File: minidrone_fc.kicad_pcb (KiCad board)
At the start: 2 copper layers, 50 x 64 mm, 40 parts, among them J1 BATT, J2 MOTOR_FL, J3 MOTOR_FR, J4 MOTOR_RL, J5 MOTOR_RR, Q1 AO3400A, Q2 AO3400A, Q3 AO3400A, Q4 AO3400A, U1 XIAO_ESP32C3, U2 GY-521, U3 BMP280

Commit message: rev2.1: 昇降圧DC-DC(TPS63002)を追加し4層化
## なぜ

改訂前の基板には昇圧素子が1つもなく、電池電圧が「3.3V + LDOドロップアウト」
を下回れば 3V3 レールは必ず追従して下がる構造だった。
8520コアレスモーター4個で 6.5A を引くと電池は 3.7V→3.4V に沈み、
そこから D5(SS24) の 0.4V を引いて VMCU ≈ 3.0V、
さらに XIAO 内蔵 LDO のドロップアウトを引くと 3V3 は 2.8〜2.95V。
ESP32-C3 の動作下限 3.0V を公称電圧ですら下回っており、
スロットルを上げた瞬間に MCU がリセットする状態だった。

## 何を変えたか

- U4 TPS63002 (昇降圧・5V固定) を VBAT と XIAO の "5V" ピンの間に挿入
  L1 2.2uH / C10 10uF(in) / C11 22uF(out) / C12 0.1uF(VINA)
  電池 3.0V でも出力5V。D5 で 0.4V 落ちても 4.6V が XIAO に入り、
  内蔵LDO が 3.3V を作るのに必要な 3.5V に対し余裕1V以上
- D5 は流用。向きも不変で、上流が VBAT から V5V に変わっただけ
- 4層化: In1.Cu = ベタGND 全面 2949mm2 / In2.Cu = VBAT プレーン 全面 2811mm2
  6.5A を 0.6mm トレースで流していた状態を解消
- GND スティッチングビア 133本を衝突判定付きで自動配置
- U4 にローカルクリアランス 0.1mm を設定
  VSON-10 は 0.5mmピッチでパッド間 0.22mm しかなく、VBAT が属する
  Power ネットクラスの 0.25mm 要求を物理的に満たせないため。
  Power の 0.25mm はモーター大電流の配線・ベタ向けポリシーであり、
  ファインピッチICのピン間に適用する意図ではない (JLCPCB 製造限界 0.1mm)

+3V3 / VMCU / GATE_* / M_* / SCL / SDA は一切変更していない。
既存部品のパッド-ネット変更は D5 pad2 の VBAT→V5V ただ1箇所。

## 検証 (kicad-cli)

                    改訂前          改訂後
  DRC 違反          32 (warning)    37 (warning) ※増分5はすべてシルク重なり
  DRC エラー        0               0
  未配線            4               1  (改善)
  schematic_parity  0               0  (回路図と基板が完全一致)
  ERC               warning 5/err 0 warning 5/err 0 (同一)

## 残課題

- 未配線1件 (GNDベタの孤立島)。電気的な害はない
- シルク警告5件。C10/C11/C12 のリファレンス文字が隣接銅箔に重なる。
  この一角は部品とビアで埋まっており逃がす余地がない
- Gerber / BOM / 実装座標は未再出力。4層として出し直しが必要
- 実機でのブラウンアウト解消は未検証

詳細は README.md 第9節と docs/superpowers/plans/2026-09-19-buckboost-and-4layer.md

Co-Authored-By: Claude Opus 5 <noreply@anthropic.com>
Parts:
- added C10: 10u, Capacitor_SMD:C_0805_2012Metric, B.Cu at (11.9, 60.8)
- added C11: 22u, Capacitor_SMD:C_0805_2012Metric, B.Cu at (18.0, 60.8)
- added C12: 0.1u, Capacitor_SMD:C_0603_1608Metric, B.Cu at (11.7, 55.5)
- added L1: 2.2uH, Inductor_SMD:L_APV_ANR3015, B.Cu at (15.0, 60.9)
- added U4: TPS63002, Package_SON:VSON-10-1EP_3x3mm_P0.5mm_EP1.65x2.4mm_ThermalVias, B.Cu at (15.0, 56.6)
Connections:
- D5 pad 2: VBAT -> V5V
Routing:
- net V5V: track 0.00 -> 15.9 mm, vias 0 -> 2
- net SW_L1: track 0.00 -> 2.95 mm
- net SW_L2: track 0.00 -> 2.95 mm
- net VBAT: track 202.7 -> 205.2 mm, vias 0 -> 3
- net GND: vias 0 -> 140
- added copper zone on In1.Cu, net GND
- added copper zone on In2.Cu, net VBAT
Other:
- copper layers 2 -> 4

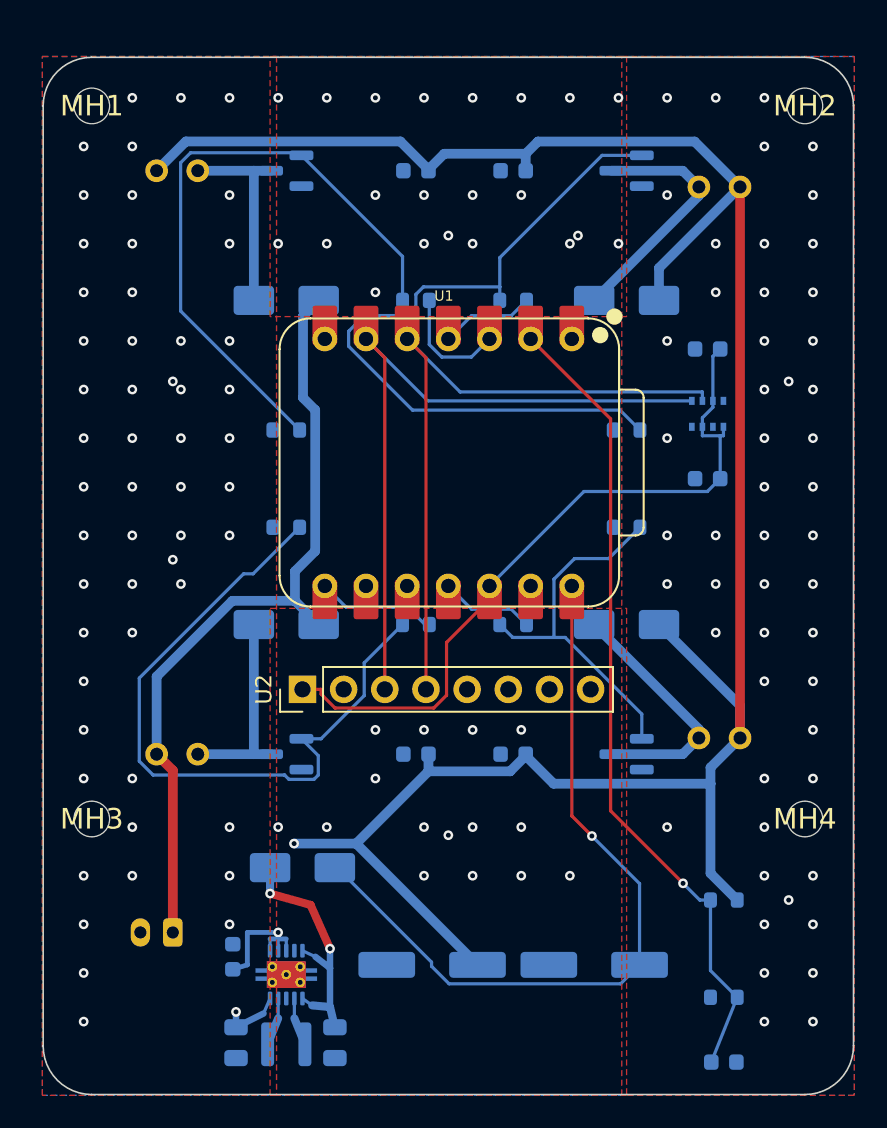
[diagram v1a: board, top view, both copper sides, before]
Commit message: rev3: 回路図を全面刷新し、29x29mm 4層基板の骨格を作成
rev2.1 (50x64mm / 取付穴44x44mm) を Tiny Whoop 標準ピッチに作り直す。
回路図は rev2 の内容を破棄して一から構成した（rev2.1 は main に保全）。

## 回路図（ERC エラー0 / 32ネット / 55部品）

  XIAO ESP32C3 (DIP) -> ESP32-C3-MINI-1 (SMD, 基板内蔵アンテナ)
  GY-521 モジュール   -> BMI270 直付け (SPI)
  BMP280              -> SPI に変更し IMU とバス共用
  TPS63002(5V)+LDO    -> TPS63001 で 3.3V 一段
  電解コンデンサ      -> 積層セラミック
  USB-C (TYPE-C-31-M-12) + USBLC6 を新規搭載

安全上の要点: 充電回路を載せないため、電池側に逆流防止ダイオード D5 を
入れて USB の 5V が LiPo に流れ込むのを防ぐ。VBAT(19ピン) と VSYS(13ピン)
が別ネットであることを確認済み（統合されると D5 が短絡し過充電になる）。

## 基板

  29 x 29 mm / 角R3 / 板厚 0.8mm / 4層
  取付穴 φ1.5mm x4 を 25.5 x 25.5mm ピッチ（Whoop 標準）
  schematic_parity: 0

## 作業中に修正した不具合

1. create_board_from_schematic が no-connect ピンに隣接ネットを割り当てた
   U1/4 -> GATE_FR, U1/7 -> GATE_RL, U2/9 -> GND, U2/11 -> GND
   rev2 でも U1/7 に GATE_RL という同一症状。再現性のある MCP の不具合。
   通常の DRC では検出できず schematic_parity でのみ分かる。
   U2/11 (OSDO) は BMI270 の出力ピンで、GND 固定のままだと危険だった。

2. D1-D4 を SS24(SMA) から DSS24(SOD-123FL) に変更
   SMA はコートヤード 7.09x3.59mm で、幅7mmの四隅に FET と同居できなかった。
   仕様書7節で想定していた置き換え。定格 2A/40V は同等、4個で 58mm² 削減。
   LCSC: C115726 -> C2923950 (在庫125,283)

3. 仕様書・計画書の J1 シンボル名の誤りを訂正
   フットプリント名を書いていた。正しくは Connector:Conn_01x02_Pin。

## 未完了

Task 9（配置）で同一面の干渉が51件残っている。
Task 10（配線）、11（DRC）、12（製造データ）は未着手。

Co-Authored-By: Claude Opus 5 <noreply@anthropic.com>
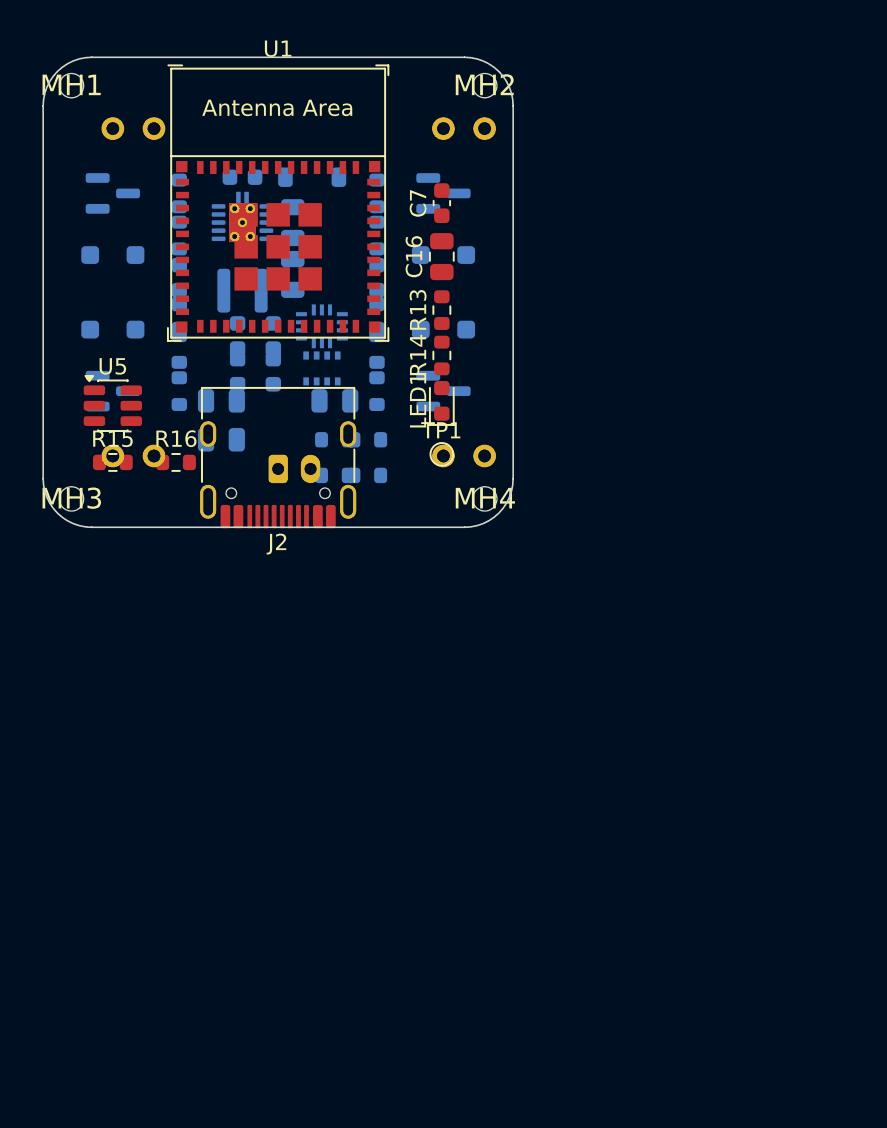
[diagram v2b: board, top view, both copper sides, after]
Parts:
- added C13: 0.1u, Capacitor_SMD:C_0603_1608Metric, B.Cu at (20.6, 13.6)
- added C14: 0.1u, Capacitor_SMD:C_0603_1608Metric, B.Cu at (8.40, 16.0)
- added C15: 0.1u, Capacitor_SMD:C_0603_1608Metric, B.Cu at (20.6, 16.0)
- added C16: 10u, Capacitor_SMD:C_0805_2012Metric, F.Cu at (24.6, 12.3)
- added J6: MOTOR_RR, TestPoint:TestPoint_2Pads_Pitch2.54mm_Drill0.8mm, B.Cu at (24.7, 24.6)
- added LED1: GREEN, LED_SMD:LED_0603_1608Metric, F.Cu at (24.6, 21.2)
- added R11: 10k, Resistor_SMD:R_0603_1608Metric, B.Cu at (20.0, 23.6)
- added R12: 10k, Resistor_SMD:R_0603_1608Metric, B.Cu at (20.0, 25.8)
- added R13: 10k, Resistor_SMD:R_0603_1608Metric, F.Cu at (24.6, 15.6)
- added R14: 1k, Resistor_SMD:R_0603_1608Metric, F.Cu at (24.6, 18.4)
- added R15: 5.1k, Resistor_SMD:R_0603_1608Metric, F.Cu at (4.30, 25.0)
- added R16: 5.1k, Resistor_SMD:R_0603_1608Metric, F.Cu at (8.20, 25.0)
- added TP1: UART_TX, TestPoint:TestPoint_Pad_D1.0mm, F.Cu at (24.6, 24.5)
- added U5: USBLC6-2SC6, Package_TO_SOT_SMD:SOT-23-6, F.Cu at (4.30, 21.5)
- C1: value 220u -> 22u; footprint Capacitor_SMD:CP_Elec_6.3x5.3 -> Capacitor_SMD:C_0805_2012Metric
- C10: value 10u -> 0.1u; footprint Capacitor_SMD:C_0805_2012Metric -> Capacitor_SMD:C_0603_1608Metric
- C11: value 22u -> 0.1u; footprint Capacitor_SMD:C_0805_2012Metric -> Capacitor_SMD:C_0603_1608Metric
- C2: value 100u -> 22u; footprint Capacitor_SMD:CP_Elec_6.3x5.3 -> Capacitor_SMD:C_0805_2012Metric
- C3, C5: value 0.1u -> 22u; footprint Capacitor_SMD:C_0603_1608Metric -> Capacitor_SMD:C_0805_2012Metric
- C4: value 0.1u -> 10u; footprint Capacitor_SMD:C_0603_1608Metric -> Capacitor_SMD:C_0805_2012Metric
- C7: moved to F.Cu
- D1, D2, D3, D4: value SS24 -> DSS24; footprint Diode_SMD:D_SMA -> D_SOD-123F
- D5: value SS24 -> B5819W; footprint Diode_SMD:D_SMA -> Diode_SMD:D_SOD-123
- J2: value MOTOR_FL -> USB-C; footprint TestPoint:TestPoint_2Pads_Pitch2.54mm_Drill0.8mm -> Connector_USB:USB_C_Receptacle_HRO_TYPE-C-31-M-12; moved to F.Cu
- J3: value MOTOR_FR -> MOTOR_FL
- J4: value MOTOR_RL -> MOTOR_FR
- J5: value MOTOR_RR -> MOTOR_RL
- MH1, MH2, MH3, MH4: value MountingHole_2.2mm -> MountingHole_1.5mm; footprint MountingHole:MountingHole_2.2mm -> MountingHole:MountingHole_1.5mm
- R3, R4, R5, R6: value 10k -> 100k
- U1: value XIAO_ESP32C3 -> ESP32-C3-MINI-1; footprint seeed:XIAO-ESP32-C3-DIP -> Espressif:ESP32-C3-MINI-1
- U2: value GY-521 -> BMI270; footprint Connector_PinHeader_2.54mm:PinHeader_1x08_P2.54mm_Vertical -> Package_LGA:Bosch_LGA-14_3x2.5mm_P0.5mm; moved to B.Cu
- U4: value TPS63002 -> TPS63001
- moved C9 52.1 mm to (12.0, 19.4), turned to 90 degrees
- moved L1 46.6 mm to (12.3, 14.4)
- moved U4 46.5 mm to (12.3, 10.2), turned to 0 degrees
- moved C10 43.7 mm to (14.2, 17.2), turned to 90 degrees
- moved D5 42.6 mm to (16.6, 7.40), turned to 0 degrees
- moved J4 42.5 mm to (24.7, 4.40)
- moved J5 42.4 mm to (4.30, 24.6), turned to 0 degrees
- moved C12 42.0 mm to (8.40, 13.6)
- moved C11 41.6 mm to (14.2, 19.4), turned to 90 degrees
- moved R2 40.2 mm to (18.0, 25.8), turned to 0 degrees
- moved C2 39.7 mm to (11.0, 23.6), turned to 0 degrees
- moved C6 39.3 mm to (12.3, 7.40), turned to 0 degrees
- moved J3 38.9 mm to (4.30, 4.40), turned to 0 degrees
- moved R1 37.2 mm to (18.0, 23.6), turned to 0 degrees
- moved C1 37.1 mm to (11.0, 21.2), turned to 0 degrees
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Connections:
- C10 pad 1: VBAT -> +3V3
- C11 pad 1: V5V -> +3V3
- C2 pad 1: VMCU -> VBAT
- C4 pad 1: VBAT -> VSYS
- C5 pad 1: VBAT -> +3V3
- C6 pad 1: VBAT -> VSYS
- C9 pad 1: BATT_SENSE -> +3V3
- D5 pad 1: VMCU -> VSYS
- D5 pad 2: V5V -> VBAT
- J3 pad 2: M_FR -> M_FL
- J4 pad 2: M_RL -> M_FR
- J5 pad 2: M_RR -> M_RL
- U1 pad 1: (no net) -> GND
- U1 pad 11: GATE_RR -> GND
- U1 pad 12: +3V3 -> BATT_SENSE
- U1 pad 13: GND -> GATE_FL
- U1 pad 14: VMCU -> GND
- U1 pad 2: BATT_SENSE -> GND
- U1 pad 3: GATE_FL -> +3V3
- U1 pad 5: SDA -> IMU_INT
- U1 pad 6: SCL -> GATE_FR
- U1 pad 7: (no net) -> GATE_RL
- U1 pad 8: GATE_RL -> +3V3
- U2 pad 1: +3V3 -> SPI_MISO
- U2 pad 2: GND -> (no net)
- U2 pad 3: SCL -> (no net)
- U2 pad 4: SDA -> IMU_INT
- U2 pad 5: (no net) -> +3V3
- U2 pad 6: (no net) -> GND
- U2 pad 7: (no net) -> GND
- U2 pad 8: (no net) -> +3V3
- U3 pad 2: +3V3 -> BARO_CS
- U3 pad 3: SDA -> SPI_MOSI
- U3 pad 4: SCL -> SPI_SCLK
- U3 pad 5: GND -> SPI_MISO
- U4 pad 1: V5V -> +3V3
- U4 pad 10: V5V -> +3V3
- U4 pad 5: VBAT -> VSYS
- U4 pad 6: VBAT -> VSYS
- U4 pad 7: VBAT -> VSYS
- U4 pad 8: VBAT -> VSYS
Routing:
- net VBAT: track 205.2 -> 0.00 mm, vias 3 -> 0
- net BATT_SENSE: track 51.4 -> 0.00 mm, vias 1 -> 0
- net VMCU: track 47.5 -> 0.00 mm, vias 1 -> 0
- net G_FR: track 46.0 -> 0.00 mm
- net +3V3: track 45.0 -> 0.00 mm
- net SCL: track 44.6 -> 0.00 mm
- net G_RL: track 43.5 -> 0.00 mm
- net SDA: track 43.1 -> 0.00 mm
- net G_FL: track 38.8 -> 0.00 mm
- net G_RR: track 22.8 -> 0.00 mm
- net V5V: track 15.9 -> 0.00 mm, vias 2 -> 0
- net M_RR: track 15.5 -> 0.00 mm
- net M_FR: track 15.5 -> 0.00 mm
- net M_RL: track 12.5 -> 0.00 mm
- net M_FL: track 12.5 -> 0.00 mm
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- removed copper zone on B.Cu, net GND
- removed copper zone on In1.Cu, net GND
- removed copper zone on F.Cu, net VBAT
- removed copper zone on In2.Cu, net VBAT
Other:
- board size 50 x 64 mm -> 29 x 29 mm
